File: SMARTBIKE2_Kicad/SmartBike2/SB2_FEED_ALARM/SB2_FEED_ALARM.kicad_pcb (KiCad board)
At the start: 2 copper layers, 45 x 45 mm, 37 parts, among them J1 Conn_01x08, J2 Conn_01x02, Q1 SI2302, Q2 FDN340P, Q3 SI2302, U1 MIC5219-3.3YM5, U2 MIC29302WU, U3 MIC5219-3.3YM5, U4 NA555D

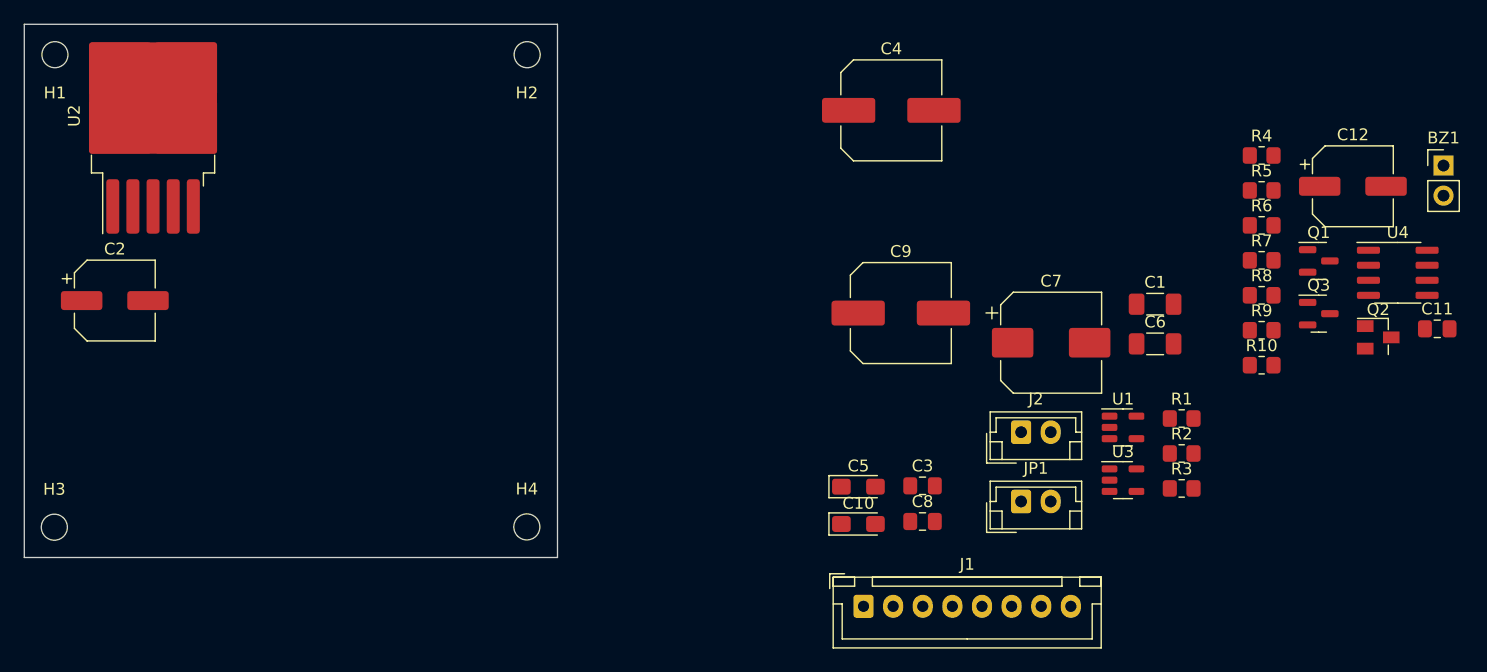
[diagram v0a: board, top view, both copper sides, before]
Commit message: Fase 2 de 3 panel
+ Esquemático Alimentación y Alarma
+ PCB 1 de 3, Alimentación y Alarma
+ Esquemático Acondicionamiento y Conexión módulos

~ PCB 2 de 3  Acondicionamiento y Conexión módulos
~ Esquemático Luces
~ PCB 3 de 3, Luces
~ Panelización
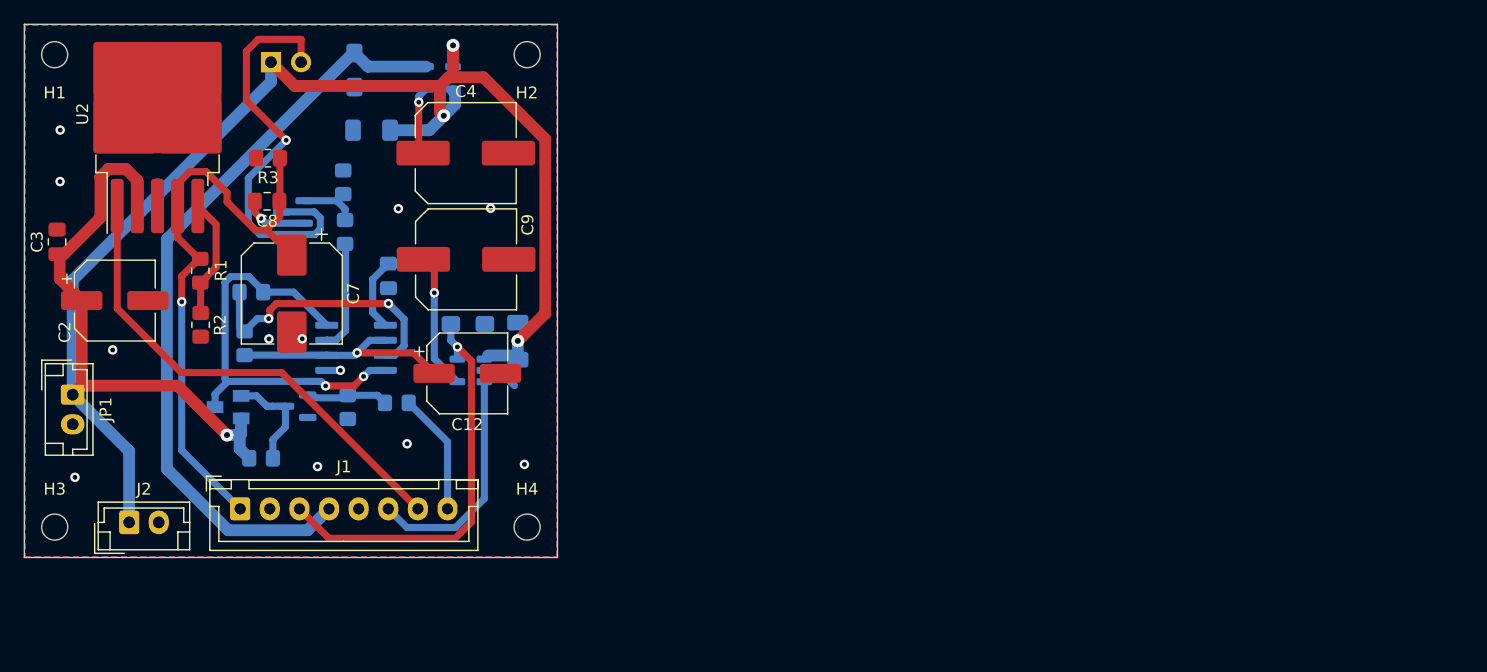
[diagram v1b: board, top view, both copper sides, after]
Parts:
- BZ1, C1, C10, C11, C5, C6, Q1, Q2, Q3, R10, R4, R5, R6, R7, R8, R9, U1, U3, U4: moved to B.Cu
- moved BZ1 99.3 mm to (35.9, 18.2), turned to -90 degrees
- moved Q2 97.2 mm to (32.3, 47.3), turned to 180 degrees
- moved C11 88.6 mm to (45.8, 36.2), turned to -90 degrees
- moved U4 88.1 mm to (43.1, 42.3)
- moved Q1 87.1 mm to (38.1, 47.2), turned to 180 degrees
- moved Q3 87.0 mm to (37.8, 30.8), turned to 180 degrees
- moved R6 86.7 mm to (35.1, 51.6)
- moved R8 85.9 mm to (33.7, 41.9), turned to -90 degrees
- moved R7 85.3 mm to (34.3, 37.6), turned to 180 degrees
- moved R1 83.8 mm to (29.9, 35.8), turned to -90 degrees
- moved R2 83.5 mm to (30.0, 40.4), turned to -90 degrees
- moved R3 82.0 mm to (35.7, 26.3), turned to 180 degrees
- moved JP1 80.5 mm to (19.2, 46.2), turned to -90 degrees
- moved R5 79.3 mm to (42.4, 47.3), turned to -90 degrees
- moved R10 79.0 mm to (42.0, 28.3), turned to 90 degrees
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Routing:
- net +5V: track 0.00 -> 157.8 mm, vias 0 -> 4
- net +3.3V: track 0.00 -> 64.8 mm
- net 4.1V: track 0.00 -> 50.9 mm, vias 0 -> 1
- net /Alimentación/ctrSIM: track 0.00 -> 41.0 mm
- net /Alarma/VA: track 0.00 -> 35.6 mm, vias 0 -> 2
- net Net-(BZ1-+): track 0.00 -> 35.2 mm, vias 0 -> 1
- net +3.3_2: track 0.00 -> 34.6 mm, vias 0 -> 1
- net GND: track 0.00 -> 29.1 mm, vias 0 -> 13
- net Net-(U4-DIS): track 0.00 -> 23.2 mm, vias 0 -> 2
- net /Alimentación/ctrGPSAc: track 0.00 -> 19.6 mm
- net /Alarma/TRIG: track 0.00 -> 19.6 mm, vias 0 -> 1
- net Net-(U3-BP): track 0.00 -> 11.5 mm, vias 0 -> 1
- net /Alarma/CtrAl: track 0.00 -> 10.3 mm
- net Net-(U2-ADJ): track 0.00 -> 10.2 mm
- net /Alarma/V5552: track 0.00 -> 9.30 mm
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- added copper zone on B.Cu, net GND
- added copper zone on F.Cu, net GND

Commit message: Fase 2 de 3 panel full
+ PCB Acondicionamiento y Módulos

~ Esquemático Luces
~ PCB 3 de 3, Luces
~ Panelización
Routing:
- net +3.3_2: track 34.6 -> 46.6 mm
- net GND: track 29.1 -> 27.0 mm, vias 13 -> 15

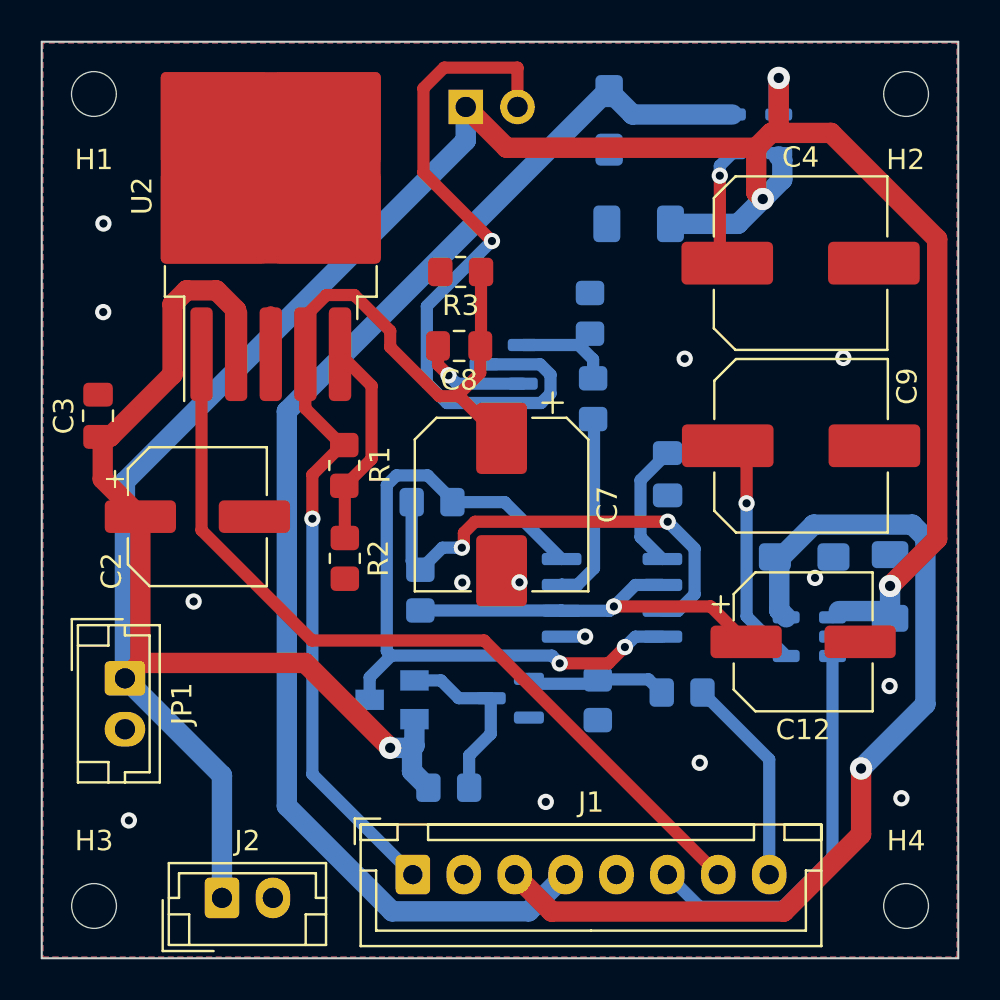
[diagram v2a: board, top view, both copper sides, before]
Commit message: Impresión vías sin metalización
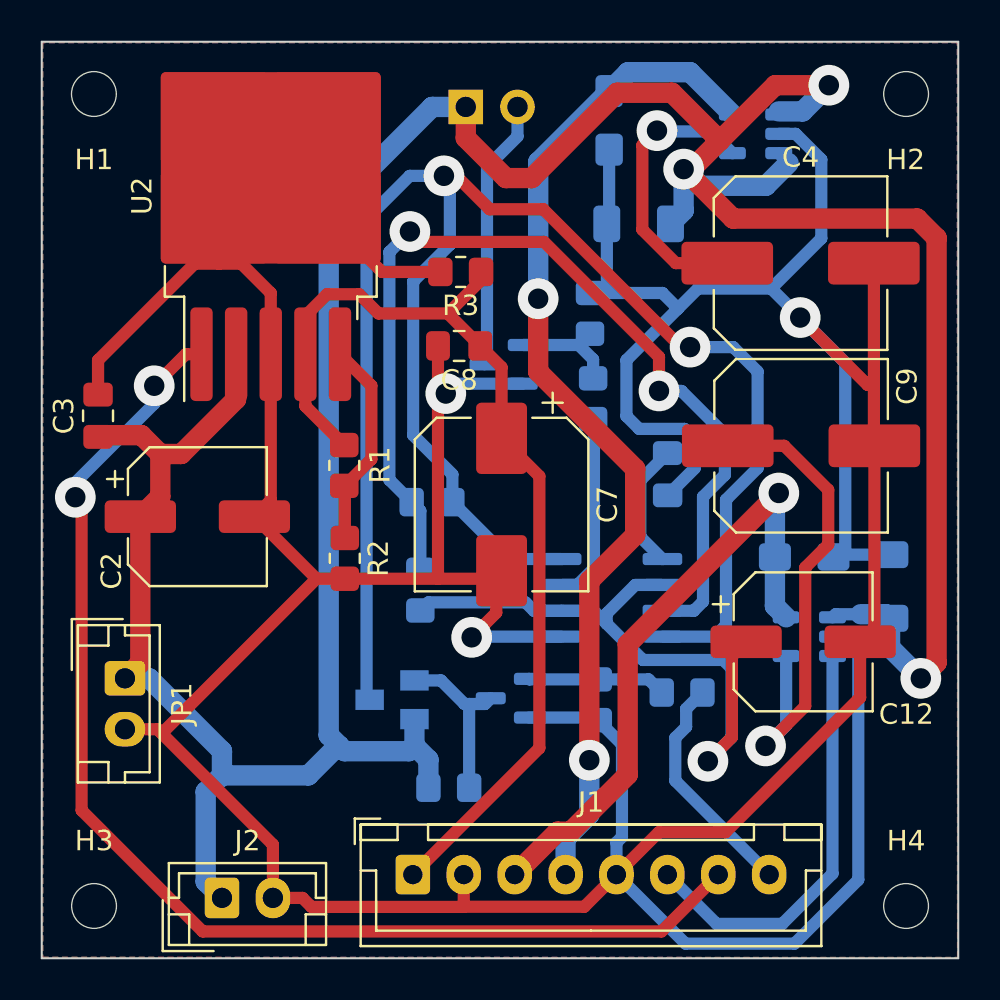
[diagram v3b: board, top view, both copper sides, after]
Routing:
- net GND: track 27.0 -> 265.8 mm, vias 15 -> 3
- net /Alarma/VA: track 35.6 -> 88.4 mm
- net Net-(U4-DIS): track 23.2 -> 49.1 mm
- net Net-(BZ1-+): track 35.2 -> 13.3 mm, vias 1 -> 0
- net /Alimentación/ctrSIM: track 41.0 -> 60.4 mm, vias 0 -> 2
- net +3.3_2: track 46.6 -> 30.9 mm
- net +3.3V: track 64.8 -> 50.6 mm, vias 0 -> 2
- net Net-(U3-BP): track 11.5 -> 24.5 mm
- net /Alarma/TRIG: track 19.6 -> 32.3 mm
- net +5V: track 157.9 -> 167.0 mm, vias 4 -> 3
- net Net-(U1-BP): track 5.81 -> 14.2 mm
- net 4.1V: track 50.9 -> 49.7 mm, vias 1 -> 0
- net /Alimentación/ctrGPSAc: track 19.6 -> 20.8 mm
- net /Alarma/CtrAl: track 10.3 -> 11.4 mm
